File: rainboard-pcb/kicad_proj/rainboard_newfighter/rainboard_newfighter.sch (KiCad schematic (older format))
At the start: 171 parts, among them J1 EJ508A, J2 USB_B, J3 Conn_01x03, J4 Conn_01x03, J5 PH2-06-UA, J6 SDS-50J, J7 SDS-50J, J8 PH2-06-UA, J9 PH2-06-UA, Q1 DUAL 30V NMOS, Q2 DUAL 30V NMOS, Q3 30V 10mOhm, U1 RT8298, U2 ATmega16U2-MU, U3 6N137, U4 74HC14, U5 ATmega16U2-MU, U6 ATmega2560-16AU, Y1 16MHz, Y2 16MHz, Y3 16MHz

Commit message: Removed RGB from buttons, part numbers updated, cleaned up schematic
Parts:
- added J? (x12): Conn_01x02_Female, symbol lib_symbol:Conn_01x02_Female
- added R? (x4): 4.7k, Resistor_SMD:R_0603_1608Metric, symbol Device:R
- added R? (x8): 19.1k, Resistor_SMD:R_0603_1608Metric, symbol Device:R
- added SW? (x4): SANWA-OBSF24, symbol lib_symbol:SANWA-OBSF24
- C12, C19, C2, C29, C31, C33, C35, C37, C40, C41, C43, C44, C46, C47, C49, C7, C9: PN (none) -> CC0603KRX7R9BB104
- C14, C20, C38: PN UWT1E471MNL1GS -> UCW1E471MNL1GS
- C32: PN DNP-UWT1E471MNL1GS -> UCW1E471MNL1GS
- FB1, FB3: PN MFBW1V3216-090-R -> 742792115
- FB2: PN MH2029-300Y -> 742792115
- J1: PN (none) -> EJ508A
- J2: PN (none) -> UJ2-BH-1-TH
- J6, J7: Field4 Manufacturer recommendations -> (none)
- JP1, JP2, JP3, JP4, JP5, TP1, TP10, TP11, TP12, TP13, TP14, TP15, TP16, TP17, TP18, TP19, TP2, TP20, TP21, TP22, TP23, TP24, TP25, TP26, TP3, TP4, TP5, TP6, TP7, TP8, TP9: PN (none) -> Virtual
- R1, R10, R11, R12, R14, R16, R2: PN (none) -> RC0603JR-07100KL
- R13, R21, R24, R27, R28, R34, R40: PN (none) -> RC0603FR-0719K1L
- R15, R23, R25, R26, R30, R5: PN (none) -> RC0603FR-07210RL
- R17, R20, R22, R29, R31, R36, R37, R38, R39, R6, R7, R8, R9: PN (none) -> RC0603JR-0711RL
- R18, R19, R3, R32, R33, R35, R4, R41: PN (none) -> RC0603JR-074K7L
- U2, U5: PN (none) -> ATMEGA16U2-MUR
- U6: PN (none) -> ATMEGA2560-16AUR
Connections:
- net 5V_MCU: now also R?.1, R?.1, R?.1, R?.1
- net BTN1a: now also R?.1
- net BTN1b: now also R?.1
- net BTN2a: now also R?.1
- net BTN2b: now also R?.1
- net BTN3a: now also R?.1
- net BTN3b: now also R?.1
- net BTN4a: now also R?.1
- net BTN4b: now also R?.1
- net BTNX-1: now also J?.1 (Pin_1)
- net BTNX-10: now also J?.1 (Pin_1)
- net BTNX-11: now also J?.1 (Pin_1)
- net BTNX-12: now also J?.1 (Pin_1)
- net BTNX-2: now also J?.1 (Pin_1)
- net BTNX-3: now also J?.1 (Pin_1)
- net BTNX-4: now also J?.1 (Pin_1)
- net BTNX-5: now also J?.1 (Pin_1)
- net BTNX-6: now also J?.1 (Pin_1)
- net BTNX-7: now also J?.1 (Pin_1)
- net BTNX-8: now also J?.1 (Pin_1)
- net BTNX-9: now also J?.1 (Pin_1)
- net GND: now also J?.2 (Pin_2), J?.2 (Pin_2), J?.2 (Pin_2), J?.2 (Pin_2), J?.2 (Pin_2), J?.2 (Pin_2), J?.2 (Pin_2), J?.2 (Pin_2), J?.2 (Pin_2), J?.2 (Pin_2), J?.2 (Pin_2), J?.2 (Pin_2), SW?.2, SW?.2, SW?.2, SW?.2
- net MetaButtons/FIRST_DIN renamed PCBMountButtons/FIRST_DIN
- new net: R?.2, R?.2, R?.2, SW?.1 (x4)
- no-connect marks 8 -> 7
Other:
- note added: "NO LEDs\nExtra HW for sharing \nbutton input"
- note added: "PCB MOUNT META BUTTONS"
- note removed: "Extra HW for sharing button input"
- note removed: "PCB MOUNT\nMETA BUTTONS"
- moved on the sheet: D14, R25, R26, R27

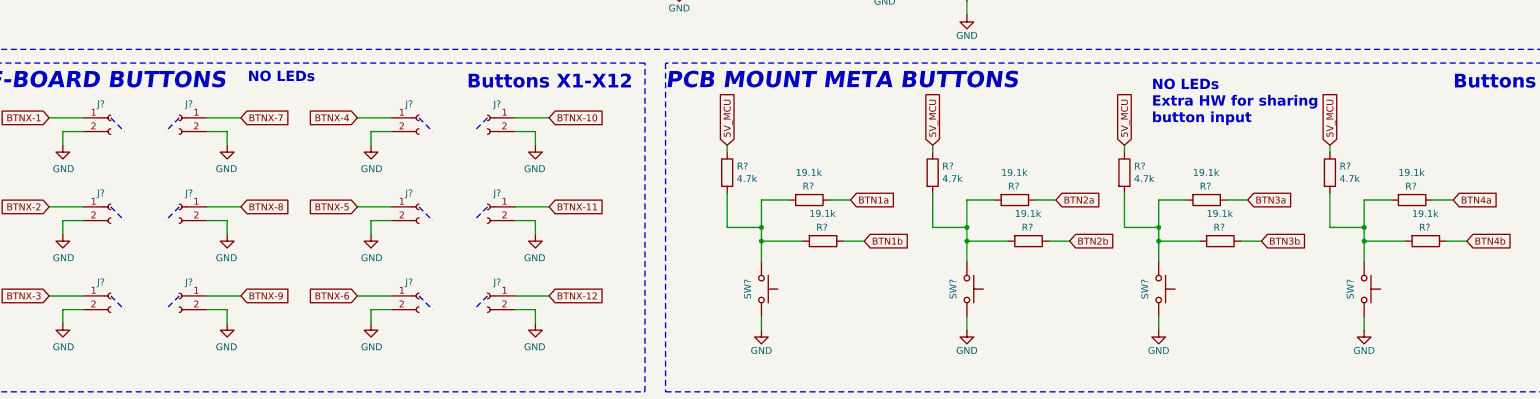
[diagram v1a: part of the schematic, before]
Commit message: New footprints added
Updated library format for footprints. Pending sync with layout to add all new footprints
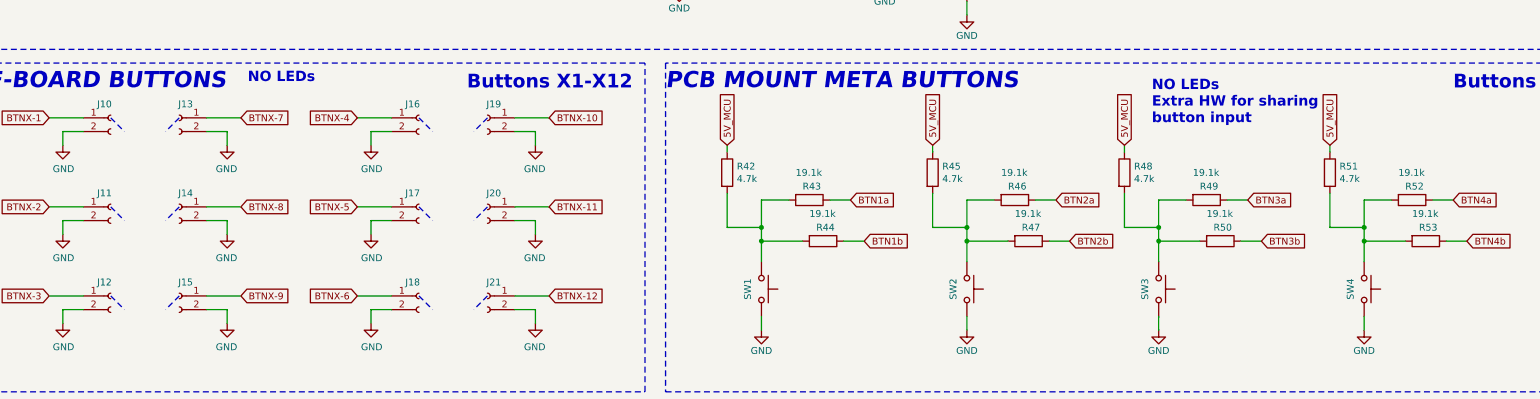
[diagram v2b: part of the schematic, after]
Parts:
- J10, J11, J12, J13, J14, J15, J16, J17, J18, J19, J20, J21: renamed from J?; footprint (none) -> Connector_JST:JST_XH_B02B-XH-A_1x02_P2.50mm_Vertical
- J2: footprint (none) -> rainboard_fp:UJ2-BH-1-TH
- J5, J8, J9: footprint (none) -> Connector_PinHeader_2.54mm:PinHeader_2x03_P2.54mm_Vertical
- J6, J7: footprint SDS-50J:CUI_SDS-50J -> rainboard_fp:CUI_SDS-50J
- L1, L3: footprint Inductor_SMD:L_Bourns_SRR1210A -> Inductor_SMD:L_12x12mm_H8mm
- L2, L4, L5: footprint (none) -> rainboard_fp:INDC250X180X200L50N
- SW1, SW2, SW3, SW4: renamed from SW?; footprint (none) -> rainboard_fp:Sanwa-OBSF24-v2
- U3: footprint (none) -> rainboard_fp:COUPL_6N138SDM
- gave numbers to parts that had none: 12

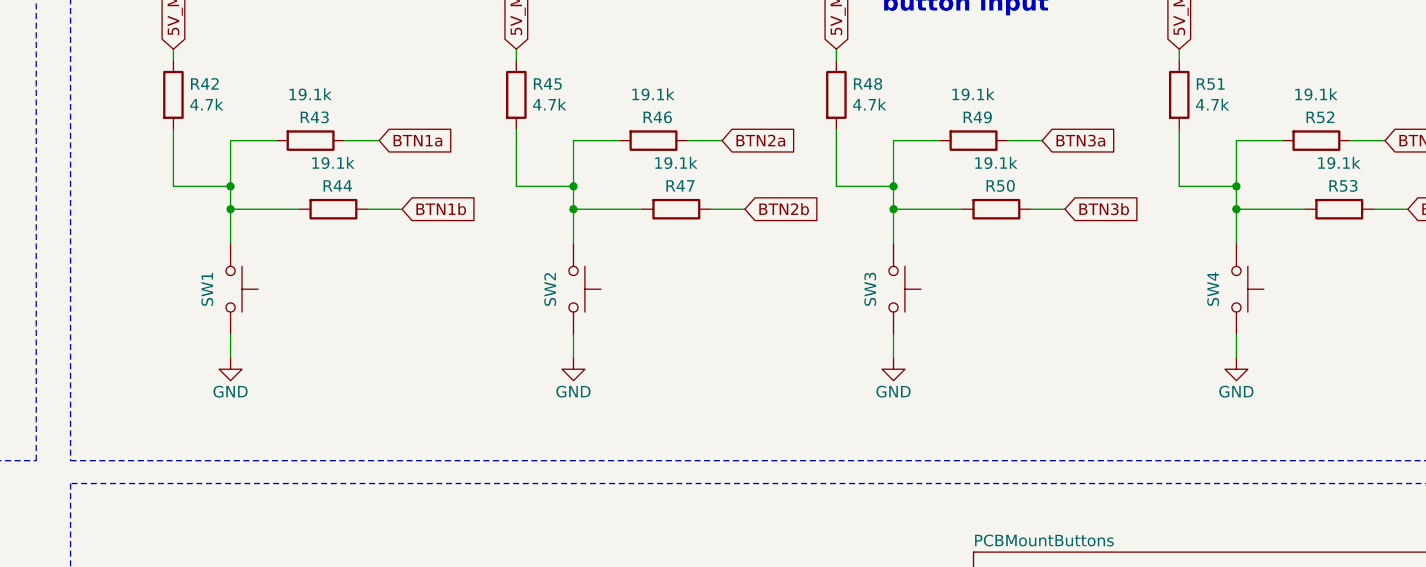
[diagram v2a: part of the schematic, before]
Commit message: Fixing annotations for buttons and meta buttons
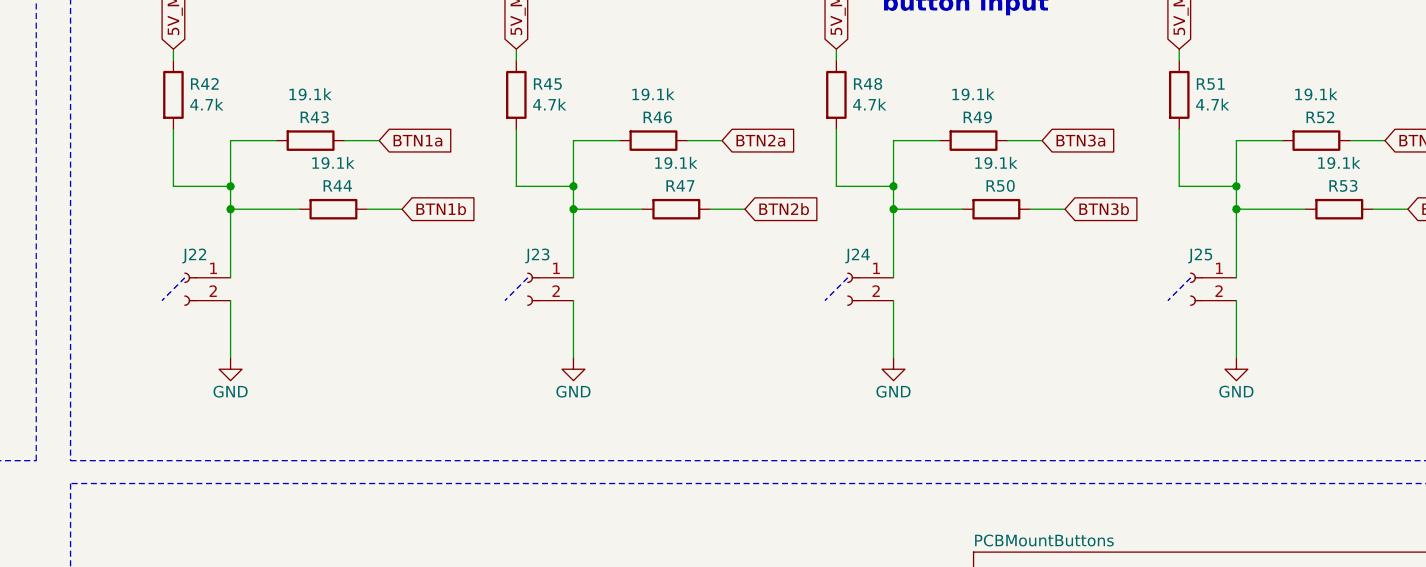
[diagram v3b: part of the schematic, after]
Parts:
- removed SW1, SW2, SW3, SW4: SANWA-OBSF24, rainboard_fp:Sanwa-OBSF24-v2, symbol lib_symbol:SANWA-OBSF24
- added J22, J23, J24, J25: Conn_01x02_Female, Connector_JST:JST_XH_B2B-XH-A_1x02_P2.50mm_Vertical, symbol lib_symbol:Conn_01x02_Female
- J10, J11, J12, J13, J14, J15, J16, J17, J18, J19, J20, J21: footprint Connector_JST:JST_XH_B02B-XH-A_1x02_P2.50mm_Vertical -> Connector_JST:JST_XH_B2B-XH-A_1x02_P2.50mm_Vertical
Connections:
- net GND: now also J22.2 (Pin_2), J23.2 (Pin_2), J24.2 (Pin_2), J25.2 (Pin_2)
- net at R42.2, R43.2, R44.2: now also J22.1 (Pin_1)
- net at R45.2, R46.2, R47.2: now also J23.1 (Pin_1)
- net at R48.2, R49.2, R50.2: now also J24.1 (Pin_1)
- net at R51.2, R52.2, R53.2: now also J25.1 (Pin_1)

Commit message: Moves meta buttons to correct config, adds back on board buttons.
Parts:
- removed J18, J19, J20, J21: Conn_01x02_Female, Connector_JST:JST_XH_B2B-XH-A_1x02_P2.50mm_Vertical, symbol lib_symbol:Conn_01x02_Female
- renumbered C4 to C1, C11 to C10, C17 to C11, C10 to C12, C12 to C13, C13 to C14, C14 to C15, C15 to C16, C34 to C17, C19 to C18, C20 to C19, C16 to C2, C21 to C20, C22 to C21, C24 to C22, C25 to C24, C26 to C25, C27 to C26, C30 to C27, C32 to C28, C2 to C29, C1 to C3, C35 to C30, C36 to C31, C33 to C32, C39 to C33, C40 to C34, C41 to C35, C45 to C36, C46 to C37, C18 to C38, C42 to C39, C3 to C4, C43 to C40, C47 to C41, C38 to C42, C48 to C43, C49 to C44, C37 to C45, C29 to C46, C50 to C47, C28 to C48, C31 to C49, C44 to C50, D11 to D10, D12 to D11, D14 to D12, D16 to D13, D7 to D14, D8 to D15, D17 to D16, D6 to D17, D13 to D3, D3 to D4, D4 to D5, D5 to D6, D9 to D7, D10 to D8, D15 to D9, J16 to J10, J17 to J11, J22 to J12, J23 to J13, J24 to J14, J7 to J15, J25 to J16, J8 to J17, J3 to J18, J4 to J19, J6 to J2, J5 to J20, J9 to J21, J2 to J3, J10 to J4, J11 to J5, J12 to J6, J13 to J7, J14 to J8, J15 to J9, JP2 to JP1, JP3 to JP2, JP1 to JP3, Q3 to Q1, Q1 to Q2, Q2 to Q3, R15 to R1, R43 to R10, R29 to R11, R44 to R12, R11 to R13, R25 to R15, R26 to R16, R16 to R17, R45 to R18, R12 to R19, R6 to R2, R13 to R20, R30 to R21, R27 to R22, R46 to R23, R47 to R24, R31 to R25, R5 to R26, R48 to R27, R49 to R28, R50 to R29, R7 to R3, R51 to R30, R52 to R31, R53 to R32, R32 to R33, R33 to R34, R1 to R35, R2 to R36, R3 to R37, R4 to R38, R21 to R39, R17 to R4, R28 to R40, R35 to R41, R36 to R42, R37 to R43, R41 to R44, R18 to R45, R19 to R46, R20 to R47, R34 to R48, R22 to R49, R8 to R5, R24 to R50, R38 to R51, R40 to R52, R39 to R53, R9 to R6, R10 to R7, R23 to R8, R42 to R9, TP10 to TP1, TP19 to TP10, TP20 to TP11, TP21 to TP12, TP22 to TP13, TP23 to TP14, TP1 to TP15, TP2 to TP16, TP24 to TP17, TP3 to TP18, TP25 to TP19, TP11 to TP2, TP26 to TP20, TP4 to TP21, TP5 to TP22, TP6 to TP23, TP7 to TP24, TP8 to TP25, TP9 to TP26, TP12 to TP3, TP13 to TP4, TP14 to TP5, TP15 to TP6, TP16 to TP7, TP17 to TP8, TP18 to TP9, U3 to U1, U1 to U2, U4 to U3, U5 to U4, U2 to U5
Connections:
- net BTNX-6: now also J7.1 (Pin_1)
- net BTNX-7: now also J8.1 (Pin_1); no longer J7.1 (Pin_1)
- net BTNX-8: now also J9.1 (Pin_1); no longer J8.1 (Pin_1)
- net GND: now also Q3.4 (S); no longer Q3.1 (S)
- net MCU1_RST: now also Q3.3 (D); no longer Q3.6 (D)
- net RST_2560: now also Q3.5 (G); no longer Q3.2 (G)
- net at TP19.1: now also Q3.6 (D); no longer Q3.3 (D)
- net at TP20.1: now also Q3.1 (S); no longer Q3.4 (S)
- net at TP17.1: now also Q3.2 (G); no longer Q3.5 (G)
- net BTNX-10 renamed BTN63
- net BTNX-11 renamed BTN65
- net BTNX-12 renamed BTN64
- net BTNX-9 renamed BTN62
- net BTN62: no longer J9.1 (Pin_1)

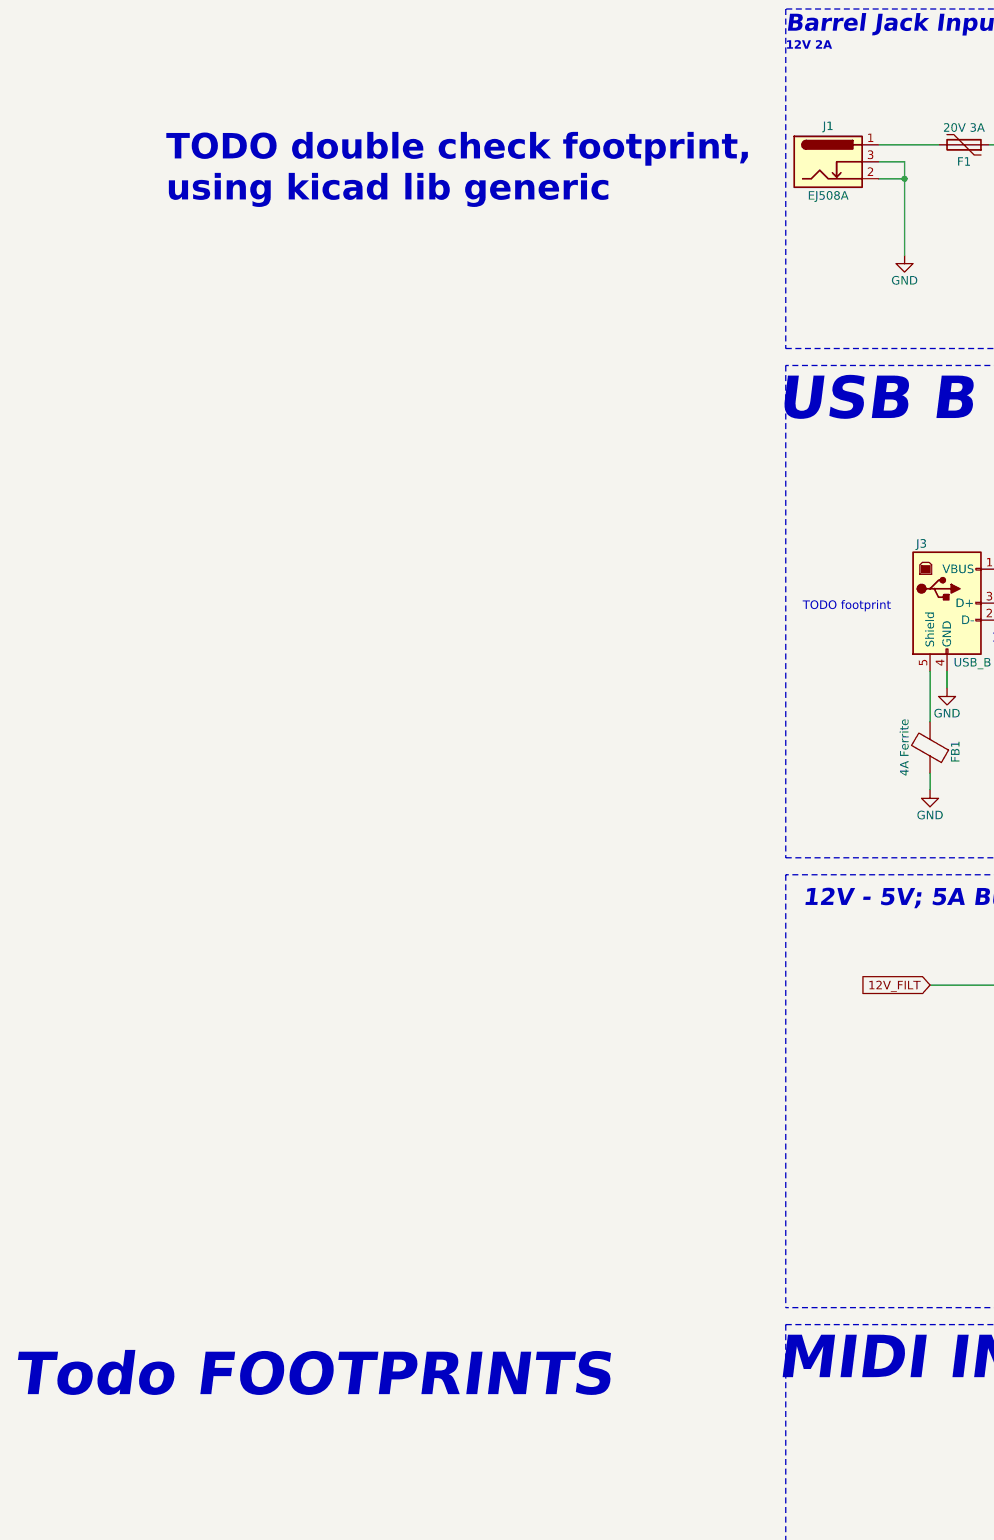
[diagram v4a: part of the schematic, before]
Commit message: Footprints fixed, button orgin moved to allow placement of LEDs
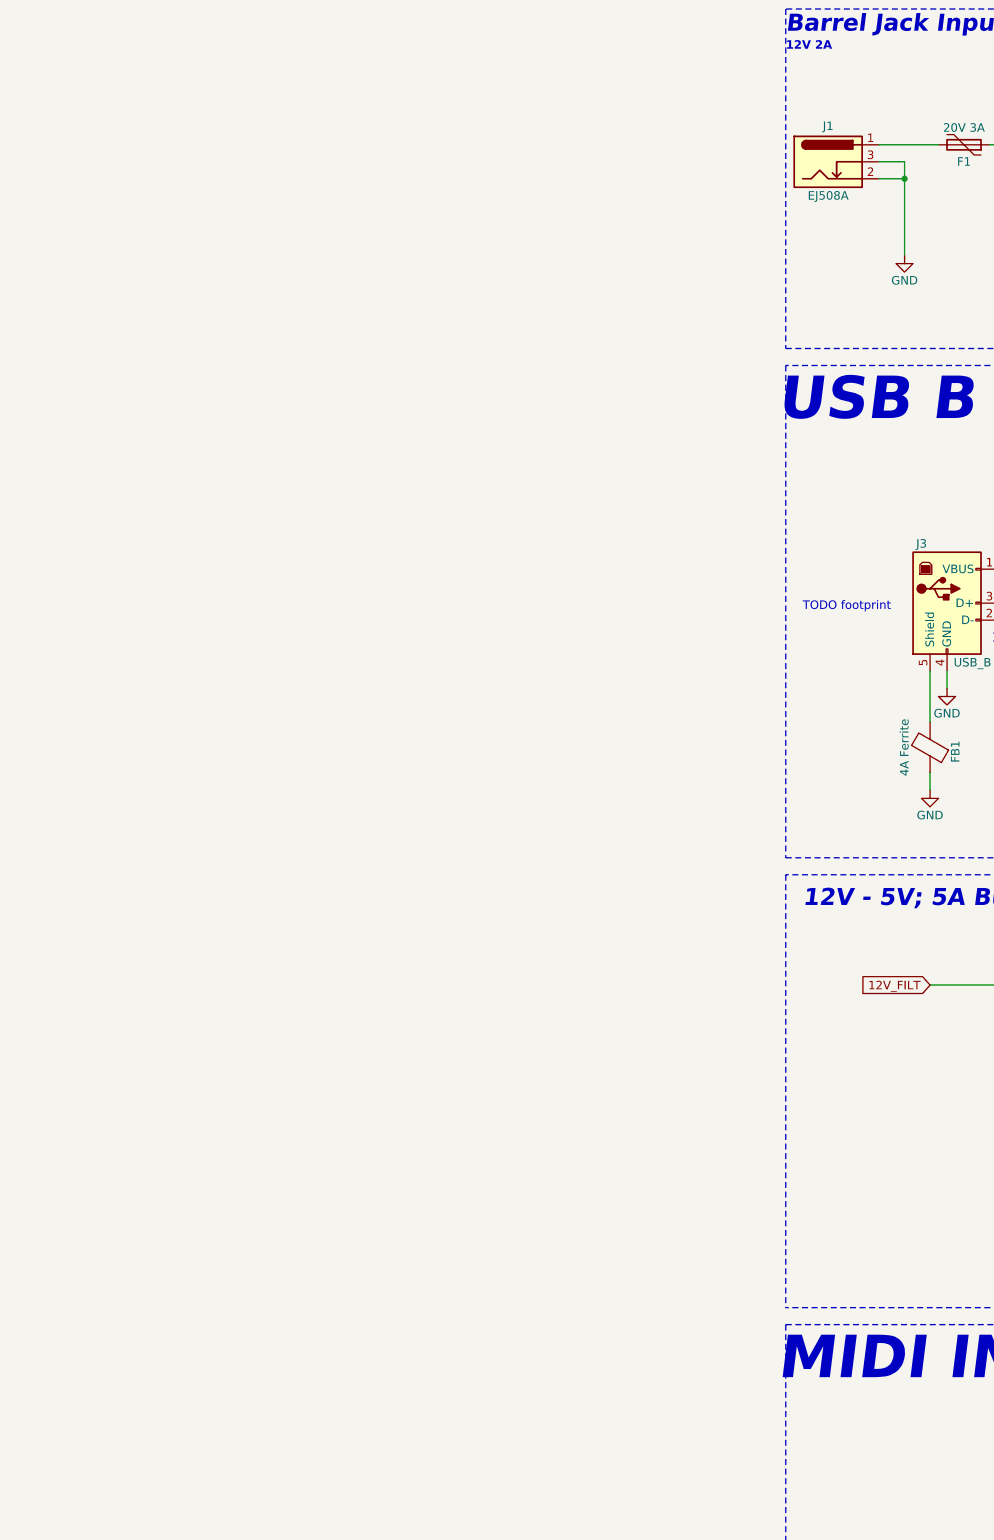
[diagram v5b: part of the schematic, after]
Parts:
- J1: footprint Connector_BarrelJack:BarrelJack_Horizontal -> rainboard_fp:BarrelJack_Horizontal
- Q1: footprint Package_SO:PowerPAK_SO-8_Single -> rainboard_fp:PowerPAK_SO-8_Single
- U2: footprint Package_SO:SOIC-8-1EP_3.9x4.9mm_P1.27mm_EP2.41x3.3mm_ThermalVias -> rainboard_fp:SOIC-8-1EP_3.9x4.9mm_P1.27mm_EP2.41x3.3mm_ThermalVias
- U4: footprint Package_DFN_QFN:QFN-32-1EP_5x5mm_P0.5mm_EP3.1x3.1mm -> rainboard_fp:QFN33P50_500X500X60L40X24T300N
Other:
- note removed: "TODO double check footprint, \nusing kicad lib generic"
- note removed: "Todo FOOTPRINTS"
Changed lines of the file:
@@
 F 0 "J1" H 800 1660 50  0000 C CNN
 F 1 "EJ508A" H 800 1250 50  0000 C CNN
-F 2 "Connector_BarrelJack:BarrelJack_Horizontal" H 850 1410 50  0001 C CNN
+F 2 "rainboard_fp:BarrelJack_Horizontal" H 850 1410 50  0001 C CNN
 F 3 "~" H 850 1410 50  0001 C CNN
 F 4 "EJ508A" H 800 1450 50  0001 C CNN "PN"
@@
 	1    0    0    -1
 $EndComp
-Text Notes -3100 1700 0    150  ~ 30
-TODO double check footprint, \nusing kicad lib generic
 Text GLabel 12100 6300 2    50   Input ~ 0
 VLED
@@
 F 0 "U2" H 4850 7150 50  0000 C CNN
 F 1 "RT8298" H 5200 7150 50  0000 C CNN
-F 2 "Package_SO:SOIC-8-1EP_3.9x4.9mm_P1.27mm_EP2.41x3.3mm_ThermalVias" H 4350 6600 50  0001 L CNN
+F 2 "rainboard_fp:SOIC-8-1EP_3.9x4.9mm_P1.27mm_EP2.41x3.3mm_ThermalVias" H 4350 6600 50  0001 L CNN
 F 3 "~" H 5100 6600 50  0001 C CNN
 F 4 "RT8298ZSP" H 5250 7250 50  0001 C CNN "PN"
@@
 F 0 "Q1" H 6250 6725 50  0000 L CNN
 F 1 "30V 10mOhm" V 6300 6150 50  0000 L CNN
-F 2 "Package_SO:PowerPAK_SO-8_Single" H 6250 6575 50  0001 L CIN
+F 2 "rainboard_fp:PowerPAK_SO-8_Single" H 6250 6575 50  0001 L CIN
 F 3 "" H 6050 6650 50  0001 L CNN
 F 4 "SI7114ADN-T1-GE3" V 6400 6350 50  0001 C CNN "PN"
@@
 F 0 "U4" H 17800 6300 50  0000 L BNN
 F 1 "ATmega16U2-MU" H 18500 3600 50  0000 L TNN
-F 2 "Package_DFN_QFN:QFN-32-1EP_5x5mm_P0.5mm_EP3.1x3.1mm" H 18400 4950 50  0001 C CIN
+F 2 "rainboard_fp:QFN33P50_500X500X60L40X24T300N" H 18400 4950 50  0001 C CIN
 F 3 "http://ww1.microchip.com/downloads/en/DeviceDoc/doc7799.pdf" H 18400 4950 50  0001 C CNN
 F 4 "ATMEGA16U2-MUR" H 18400 4950 50  0001 C CNN "PN"
@@
 	0    -1   -1   0
 $EndComp
-Text Notes -4000 8750 0    250  Italic 50
-Todo FOOTPRINTS
 Text Notes 18650 12800 0    50   ~ 0
 512 B RAM\n73 LEDs = 73x3 = 219B needed to store all LEDs

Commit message: Swaps over to 5V  input supply
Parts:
- removed C12, C16, C20, C8: 1uF 25V, Capacitor_SMD:C_0805_2012Metric, symbol lib_symbol:C
- removed C21, C22, C24, C25, C26, C27, C3, C4, C6: 10uF 25V, Capacitor_SMD:C_1206_3216Metric, symbol lib_symbol:C
- removed C28: 470uF 25V, Capacitor_SMD:CP_Elec_10x10, symbol lib_symbol:CP
- removed C9: 100nf, Capacitor_SMD:C_0603_1608Metric, symbol Device:C
- removed D1: 12Vw, Diode_SMD:D_SMA, symbol lib_symbol:D_Zener
- removed D8: 40V 1A, Diode_SMD:D_SOD-123, symbol lib_symbol:D_Schottky
- removed L3: 27uH, Inductor_SMD:L_12x12mm_H8mm, symbol lib_symbol:L
- removed Q1: 30V 10mOhm, rainboard_fp:PowerPAK_SO-8_Single, symbol lib_symbol:NMOS_SGD_123_4_5
- removed R13, R17, R19, R7: 100k, Resistor_SMD:R_0603_1608Metric, symbol Device:R
- removed R20: 19.1k, Resistor_SMD:R_0603_1608Metric, symbol Device:R
- removed U2: RT8298, rainboard_fp:SOIC-8-1EP_3.9x4.9mm_P1.27mm_EP2.41x3.3mm_ThermalVias, symbol lib_symbol:RT8298
- added D1: 6V, rainboard_fp:SOT23-3, symbol lib_symbol:D_Zener_SOT23
- F1: value 20V 3A -> 12V 5A; footprint Fuse:Fuse_1812_4532Metric -> Fuse:Fuse_2010_5025Metric; PN TLC-MSMD150/20 -> MF-USML550/12-2
- FB2: value 4A Ferrite -> 10A Ferrite; footprint Inductor_SMD:L_1206_3216Metric -> Inductor_SMD:L_1210_3225Metric; PN 742792115 -> BLE32PN300SN1L
- J1: value EJ508A -> 54-00167; PN EJ508A -> 54-00167
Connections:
- net 5V_POW is gone; now on net 5V_WALL: JP1.1, L4.2
- net GND: now also D1.1 (K), D1.2 (A)
- net at C5.1, C7.1, F1.1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: now also D1.3 (NC)
- net 12V_FILT renamed 5V_WALL
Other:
- note added: "5V 8A JACK"
- note added: "60mA each LED, \nx61 = 3.7A maximum"
- note added: "D1 handles transients, and will \ntrip fuse if 12V supply is used"
- note removed: "12V - 5V; 5A Buck"
- note removed: "12V 2A"
- note removed: "50mA each LED, \nx61 = 3A minimum"
- note removed: "Place if Ceramic Caps\nMake noise from RBG PWM"
- note removed: "Schottky Optional for\nBetter Efficiency"
- note removed: "TODO:\nI'm not sure ESD protection here is right,\nwhat exactly is softpot? \n\nQUESTION:potentiometer INPUT or simulated potentiometer output???"
- moved on the sheet: C1, C11, C17, C18, C2, D12, D13, D3, D9, J10, J11, J12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
